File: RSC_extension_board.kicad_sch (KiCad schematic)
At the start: 32 parts, among them J1 Conn_01x02, J10 Conn_01x03, J11 Conn_01x10, J15 Conn_02x20_Odd_Even, J17 TSM-120-01-L-DH-A-K-TR, J18 NPTC202KFMS-RC, J2 Raspberry_Pi_4, J3 Conn_01x02, J4 Conn_01x03, J5 Conn_01x03, J6 Conn_01x03, J7 PRT-14417, J8 Conn_01x04, J9 Conn_01x03, Q1 2N7002-7-F, Q2 BSS138

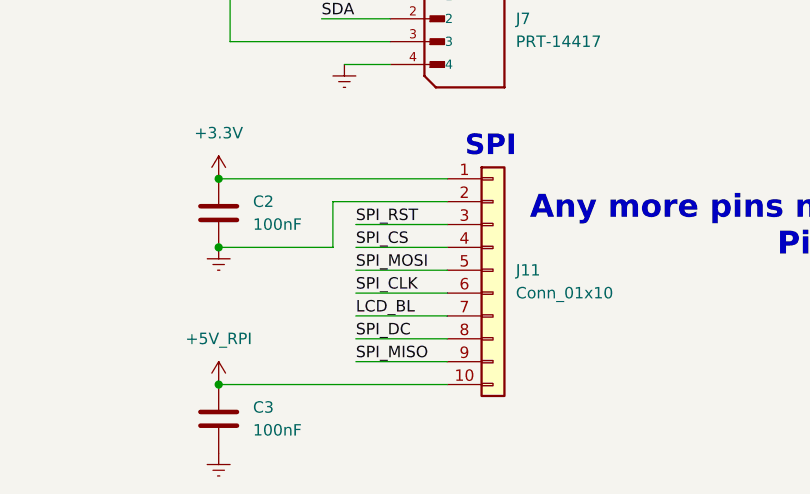
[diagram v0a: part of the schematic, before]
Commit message: spi connector pin order. bit of routing
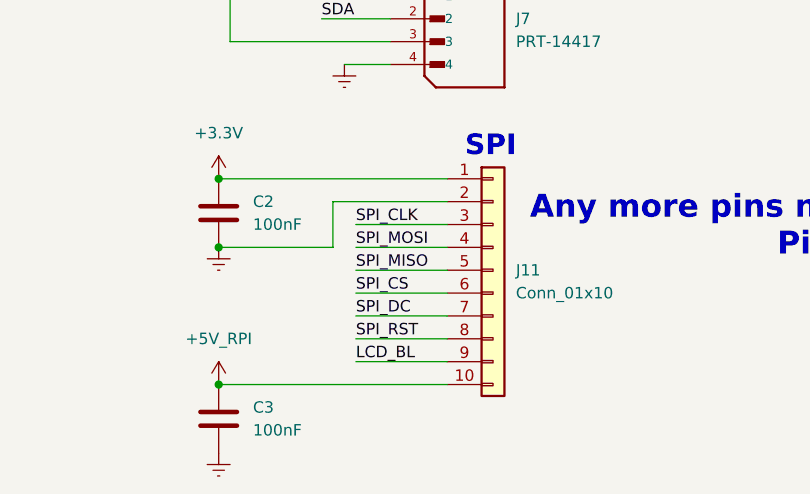
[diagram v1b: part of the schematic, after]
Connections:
- net LCD_BL: now also J11.9 (Pin_9); no longer J11.7 (Pin_7)
- net SPI_CLK: now also J11.3 (Pin_3); no longer J11.6 (Pin_6)
- net SPI_CS: now also J11.6 (Pin_6); no longer J11.4 (Pin_4)
- net SPI_DC: now also J11.7 (Pin_7); no longer J11.8 (Pin_8)
- net SPI_MISO: now also J11.5 (Pin_5); no longer J11.9 (Pin_9)
- net SPI_MOSI: now also J11.4 (Pin_4); no longer J11.5 (Pin_5)
- net SPI_RST: now also J11.8 (Pin_8); no longer J11.3 (Pin_3)

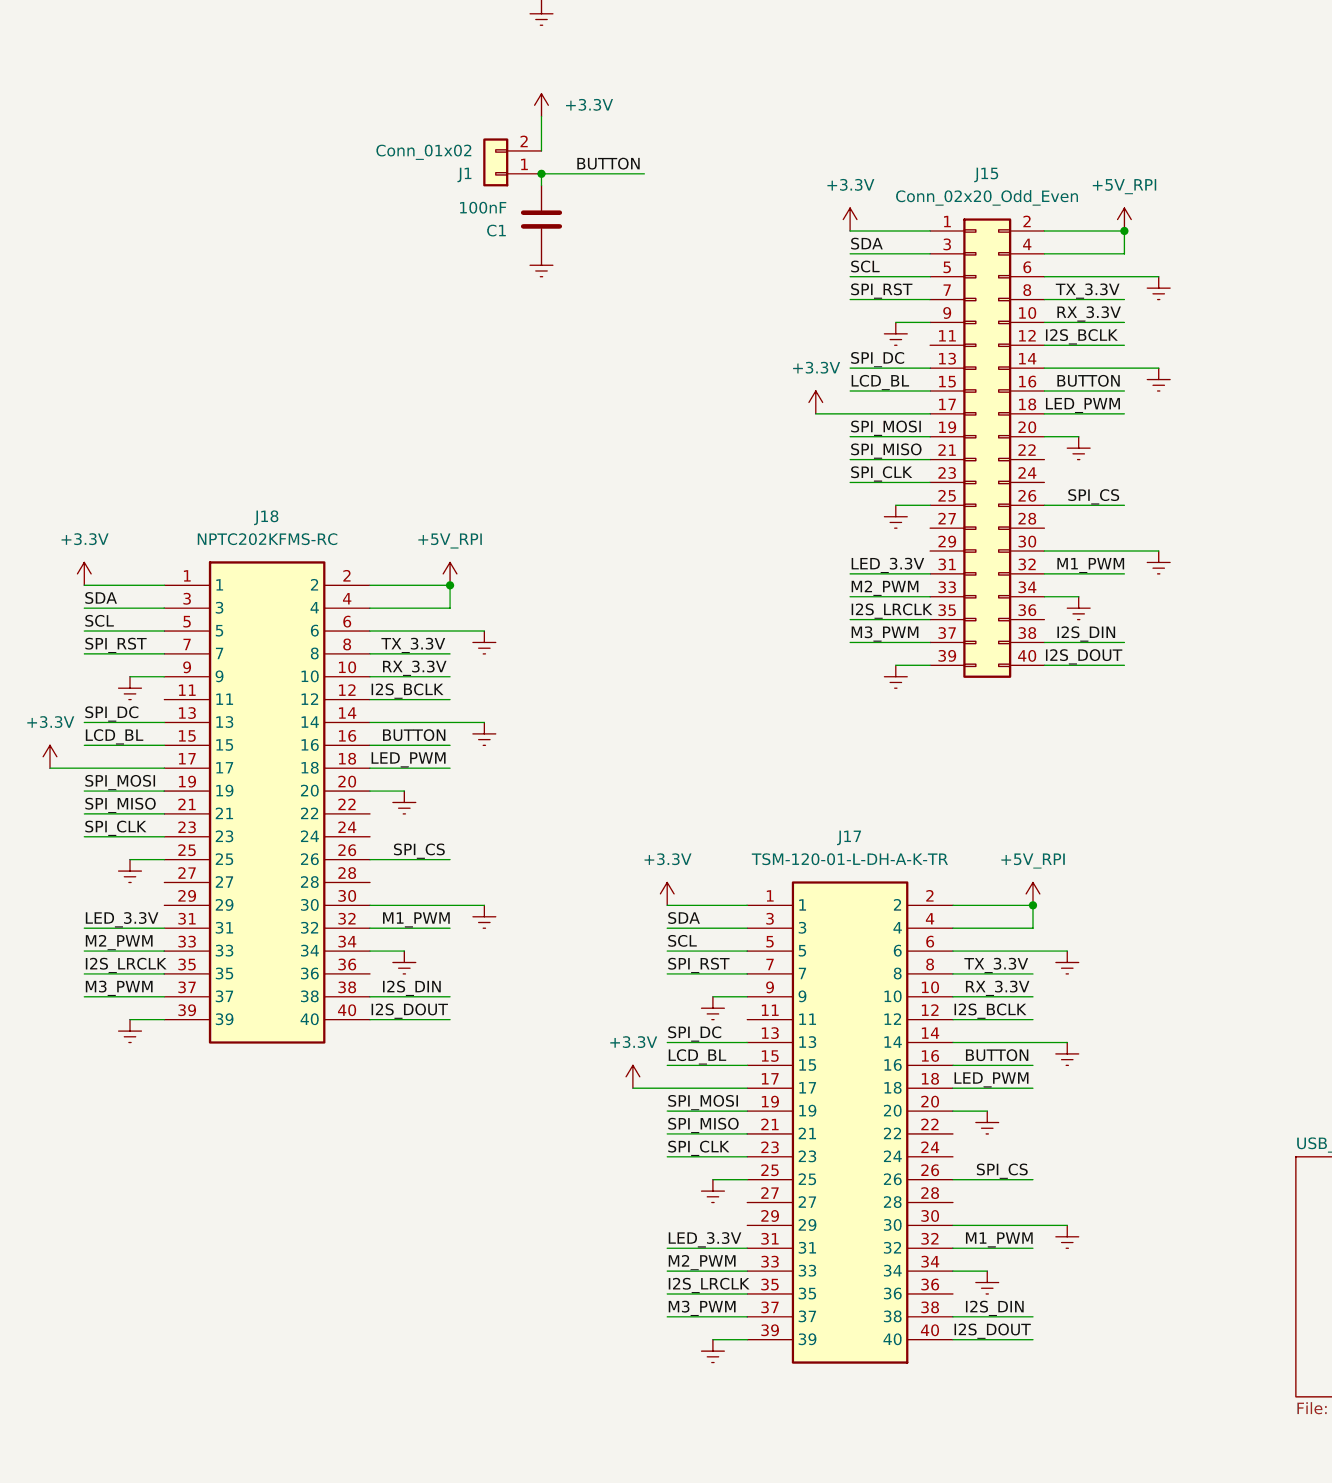
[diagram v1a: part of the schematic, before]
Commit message: all nets for headers
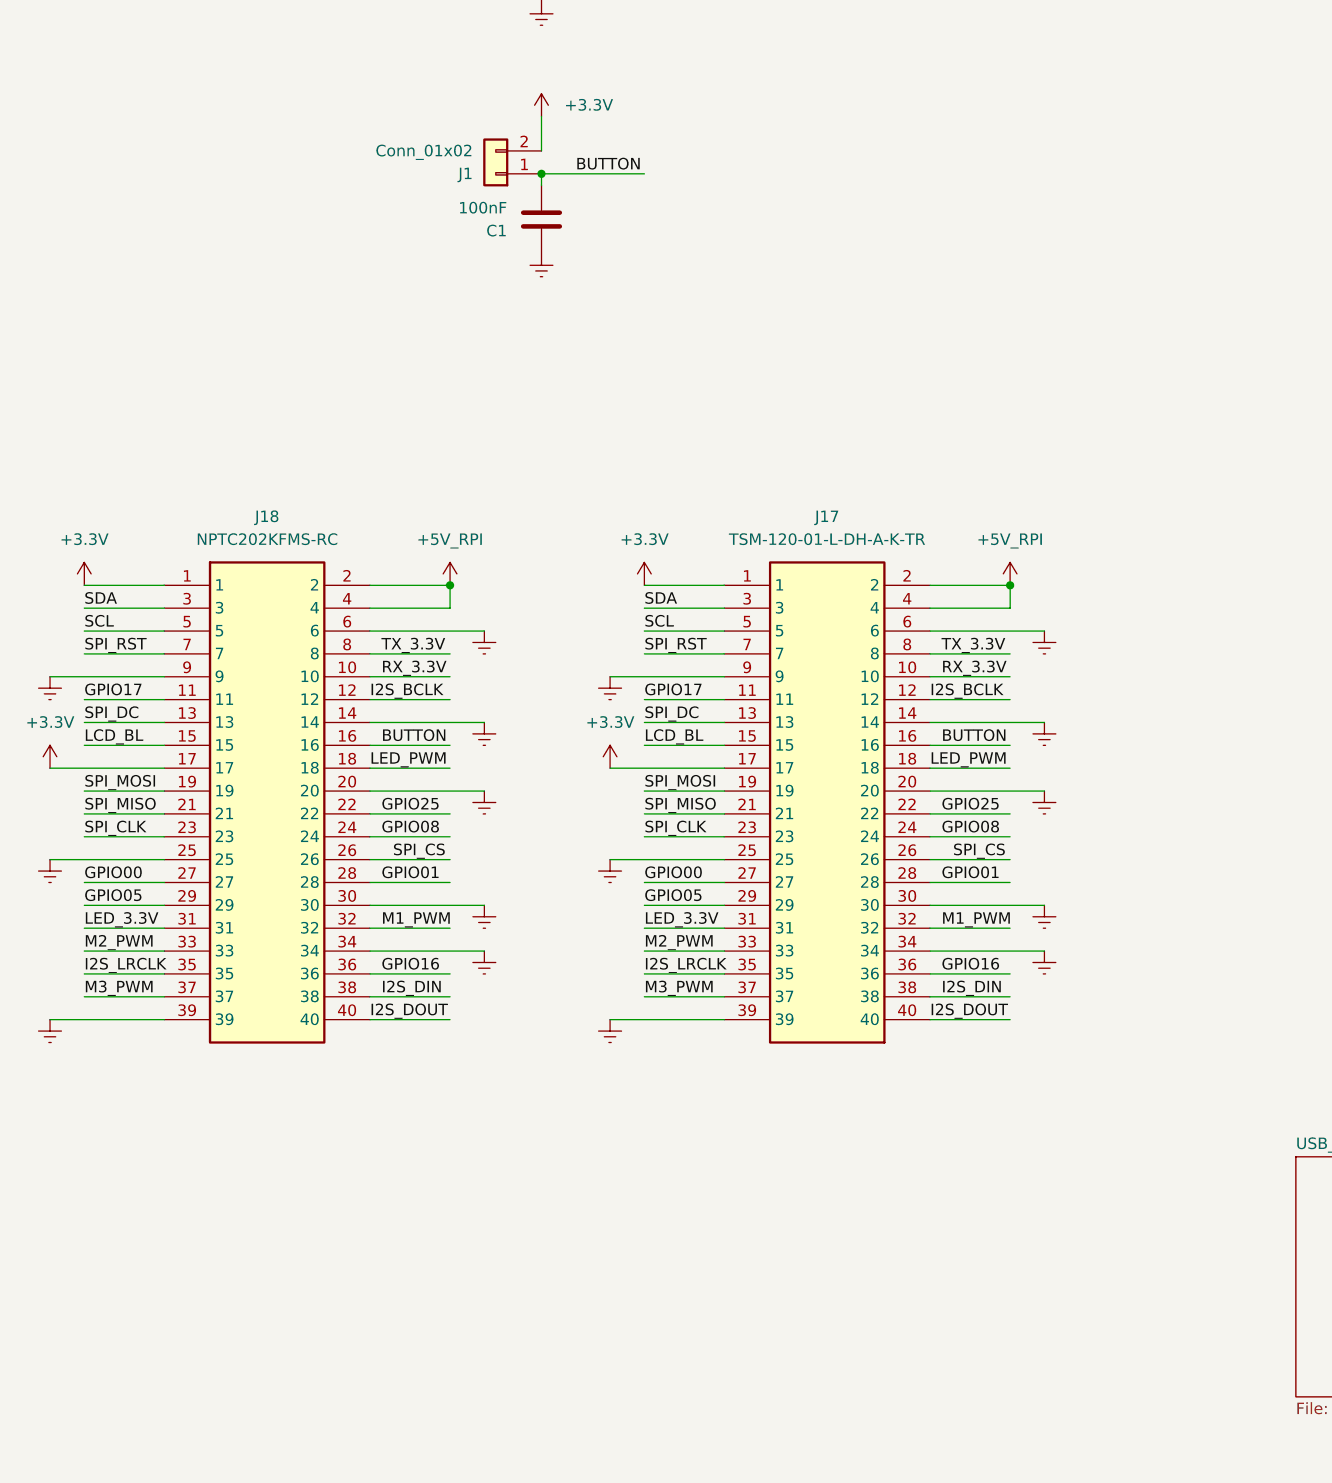
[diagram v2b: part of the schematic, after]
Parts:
- removed J15: Conn_02x20_Odd_Even, Connector_PinHeader_2.54mm:PinHeader_2x20_P2.54mm_Horizontal, symbol Connector_Generic:Conn_02x20_Odd_Even
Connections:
- net GPIO17: now reaches J18.11
- net GPIO17: now also J17.11
- net GPIO25: now reaches J18.22
- net GPIO25: now also J17.22
- net GPIO08: now reaches J18.24
- net GPIO08: now also J17.24
- net GPIO00: now reaches J18.27
- net GPIO00: now also J17.27
- net GPIO01: now reaches J18.28
- net GPIO01: now also J17.28
- net GPIO05: now reaches J18.29
- net GPIO05: now also J17.29
- net GPIO16: now reaches J18.36
- net GPIO16: now also J17.36
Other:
- moved on the sheet: J17

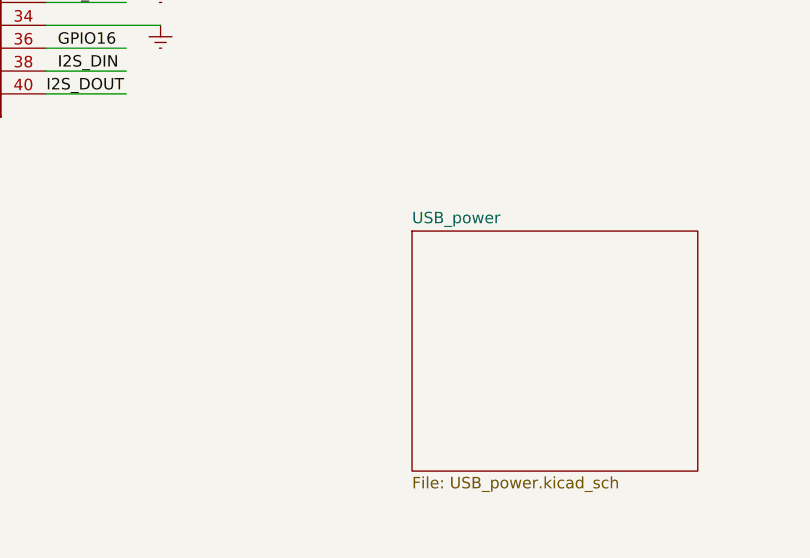
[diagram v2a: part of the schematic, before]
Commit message: bit wider power tracks
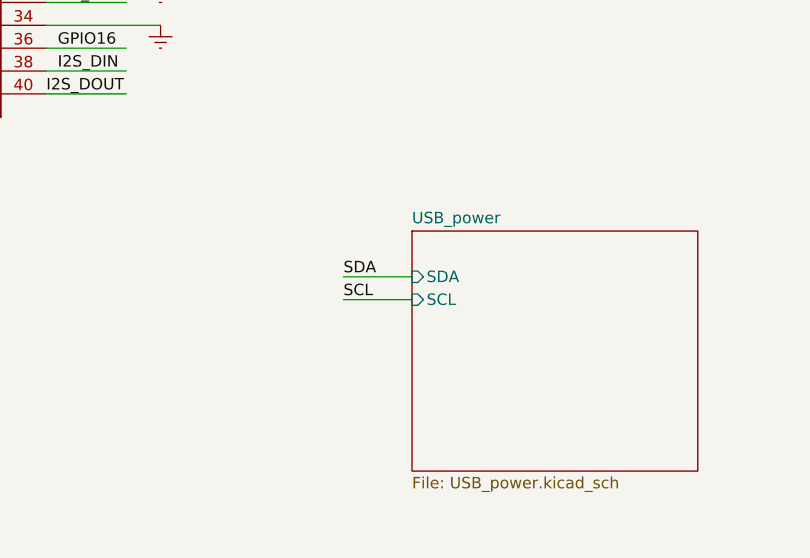
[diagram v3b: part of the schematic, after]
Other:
- sheet USB_power ports: added SCL, SDA; removed none
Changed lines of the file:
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@@
 	(wire
 		(pts
+			(xy 148.59 214.63) (xy 156.21 214.63)
+		)
+		(stroke
+			(width 0)
+			(type default)
+		)
+	)
+	(wire
+		(pts
+			(xy 148.59 217.17) (xy 156.21 217.17)
+		)
+		(stroke
+			(width 0)
+			(type default)
+		)
+	)
+	(wire
+		(pts
 			(xy 342.9 133.35) (xy 367.03 133.35)
 		)
@@
 		)
 	)
+	(label "SDA"
+		(at 148.59 214.63 0)
+		(effects
+			(font
+				(size 1.27 1.27)
+			)
+			(justify left bottom)
+		)
+	)
 	(label "LED_3.3V"
 		(at 107.95 58.42 0)
@@
 		)
 	)
+	(label "SCL"
+		(at 148.59 217.17 0)
+		(effects
+			(font
+				(size 1.27 1.27)
+			)
+			(justify left bottom)
+		)
+	)
 	(label "GPIO08"
 		(at 54.61 173.99 0)
@@
 			)
 		)
+		(pin "SCL" input
+			(at 156.21 217.17 180)
+			(effects
+				(font
+					(size 1.27 1.27)
+				)
+				(justify left)
+			)
+		)
+		(pin "SDA" input
+			(at 156.21 214.63 180)
+			(effects
+				(font
+					(size 1.27 1.27)
+				)
+				(justify left)
+			)
+		)

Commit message: pull down resistor on PD mosfet gates- for jumper
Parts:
- renumbered J18 to J1, J8 to J10, J9 to J11, J10 to J12, J11 to J13, J1 to J2, J2 to J3, J17 to J4, J3 to J5, J4 to J6, J5 to J7, J6 to J8, J7 to J9, JP3 to JP1
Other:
- note removed: "Any more pins needed for spi display? Pin order?"

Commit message: bit better gnd plane. some silkscreen
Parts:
- G1: footprint (none) -> SparkFun-Qwiic:qwiic_5mm
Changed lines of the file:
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@@
 		(exclude_from_sim no)
 		(in_bom yes)
-		(on_board no)
+		(on_board yes)
 		(dnp no)
 		(fields_autoplaced yes)
@@
 			)
 		)
-		(property "Footprint" ""
+		(property "Footprint" "SparkFun-Qwiic:qwiic_5mm"
 			(at 369.57 190.5 0)
 			(effects

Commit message: silkscreen: logo, text, testpads.
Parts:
- removed J3: Raspberry_Pi_4, KiCad:M207812045R_bottomLayer, symbol Connector:Raspberry_Pi_4
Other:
- note removed: "Pins need confirmation!!!"
- moved on the sheet: C1, J1, J2, J4

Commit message: generic 2.54mm headers and testPads excluded from BOM
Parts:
- G1, J10, J11, J12, J13, J2, J5, J6, J7, J8: now left out of the parts list
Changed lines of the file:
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@@
 		(unit 1)
 		(exclude_from_sim no)
-		(in_bom yes)
+		(in_bom no)
 		(on_board yes)
 		(dnp no)
@@
 		(unit 1)
 		(exclude_from_sim no)
-		(in_bom yes)
+		(in_bom no)
 		(on_board yes)
 		(dnp no)
@@
 		(unit 1)
 		(exclude_from_sim no)
-		(in_bom yes)
+		(in_bom no)
 		(on_board yes)
 		(dnp no)
@@
 		(unit 1)
 		(exclude_from_sim no)
-		(in_bom yes)
+		(in_bom no)
 		(on_board yes)
 		(dnp no)
@@
 		(unit 1)
 		(exclude_from_sim no)
-		(in_bom yes)
+		(in_bom no)
 		(on_board yes)
 		(dnp no)
@@
 		(unit 1)
 		(exclude_from_sim no)
-		(in_bom yes)
+		(in_bom no)
 		(on_board yes)
 		(dnp no)
@@
 		(unit 1)
 		(exclude_from_sim no)
-		(in_bom yes)
+		(in_bom no)
 		(on_board yes)
 		(dnp no)
@@
 		(unit 1)
 		(exclude_from_sim no)
-		(in_bom yes)
+		(in_bom no)
 		(on_board yes)
 		(dnp no)
@@
 		(unit 1)
 		(exclude_from_sim no)
-		(in_bom yes)
+		(in_bom no)
 		(on_board yes)
 		(dnp no)
@@
 		(unit 1)
 		(exclude_from_sim no)
-		(in_bom yes)
+		(in_bom no)
 		(on_board yes)
 		(dnp no)

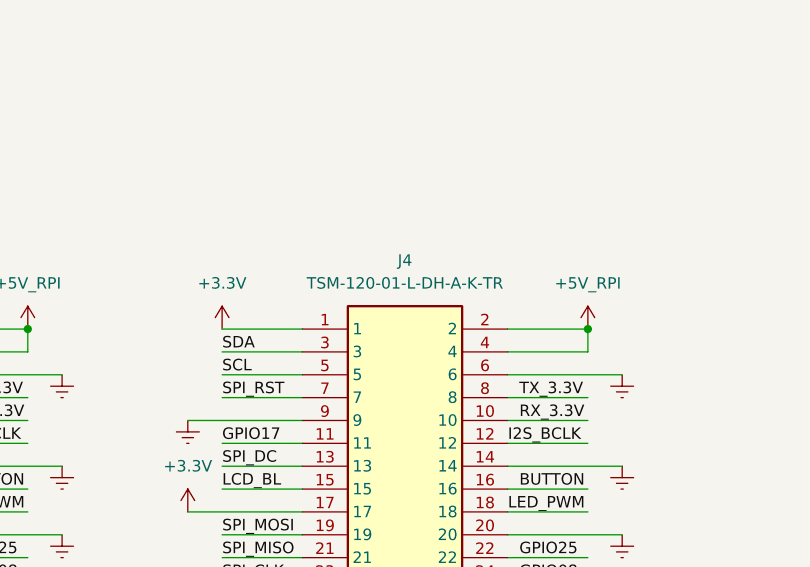
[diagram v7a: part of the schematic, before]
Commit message: J4 connector had correct footprint but false component name
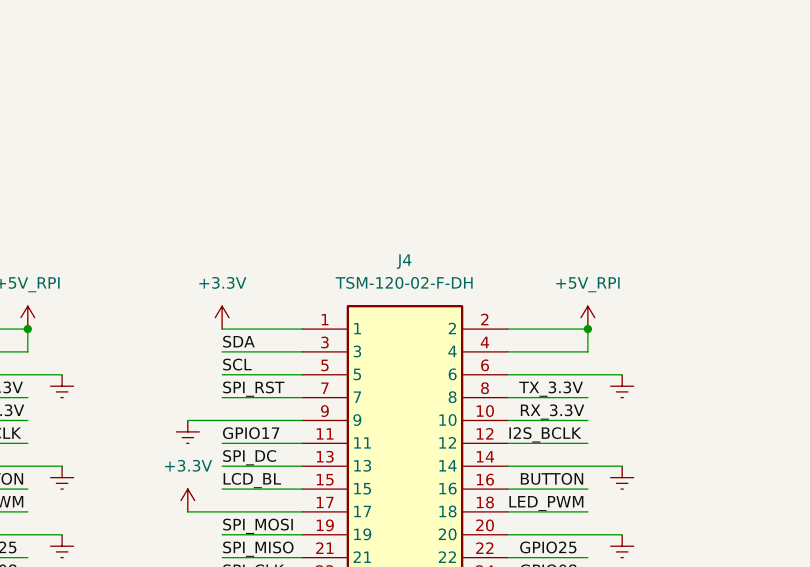
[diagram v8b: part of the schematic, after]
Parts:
- J4: value TSM-120-01-L-DH-A-K-TR -> TSM-120-02-F-DH; Manufacturer_Part_Number TSM-120-01-L-DH-A-K-TR -> TSM-120-02-F-DH; Mouser Part Number 200-TSM12001LDHAKTR -> 200-TSM12002FDH; Mouser Price/Stock https://www.mouser.co.uk/ProductDetail/Samtec/TSM-120-01-L-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 -> (none)
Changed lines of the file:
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@@
 			)
 		)
-		(property "Value" "TSM-120-01-L-DH-A-K-TR"
+		(property "Value" "TSM-120-02-F-DH"
 			(at 123.19 48.26 0)
 			(effects
@@
 			)
 		)
-		(property "Manufacturer_Part_Number" "TSM-120-01-L-DH-A-K-TR"
+		(property "Manufacturer_Part_Number" "TSM-120-02-F-DH"
 			(at 115.57 -493.32 0)
 			(effects
@@
 			)
 		)
-		(property "Mouser Part Number" "200-TSM12001LDHAKTR"
+		(property "Mouser Part Number" "200-TSM12002FDH"
 			(at 115.57 -593.32 0)
 			(effects
@@
 			)
 		)
-		(property "Mouser Price/Stock" "https://www.mouser.co.uk/ProductDetail/Samtec/TSM-120-01-L-DH-A-K-TR?qs=Cqqh%252BS766wkIdpcdtjp1jQ%3D%3D"
+		(property "Mouser Price/Stock" ""
 			(at 115.57 -693.32 0)
 			(effects
